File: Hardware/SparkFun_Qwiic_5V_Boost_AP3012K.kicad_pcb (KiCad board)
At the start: 2 copper layers, 25.4 x 25.4 mm, 65 parts, among them J1 Qwiic_RA, J2 Qwiic_RA, J3 Conn_01x06, Q1 BSS138, Q2 BSS138, U5 AP3012

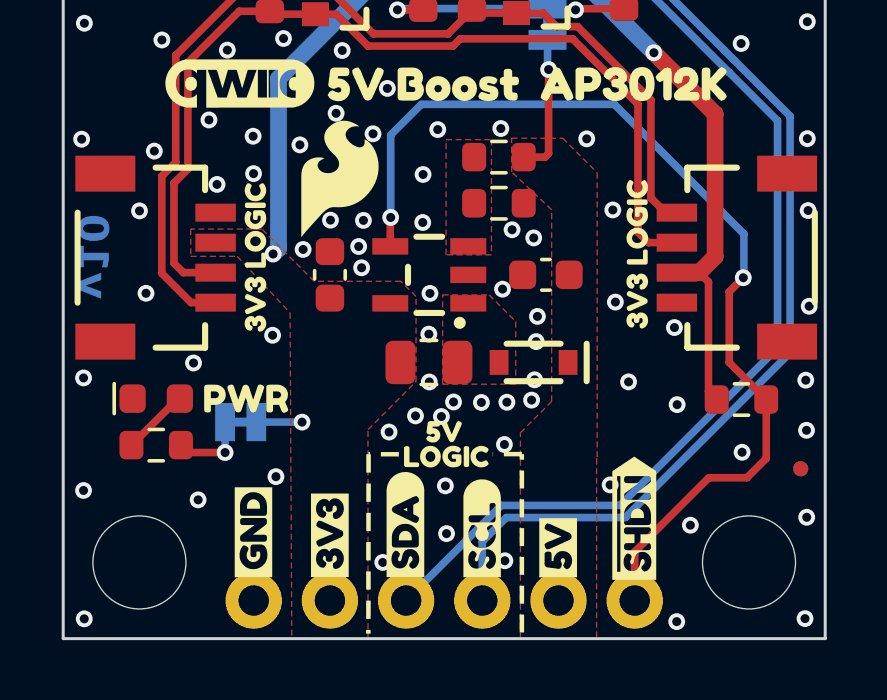
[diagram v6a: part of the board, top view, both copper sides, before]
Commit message: buzzard label adjustments
-extended left side spacing of PTH buzzard labels to 6mils
-positioned them so they clear the PTH header plastic molding courtyard
-snapped them all to a 6.25mils grid.
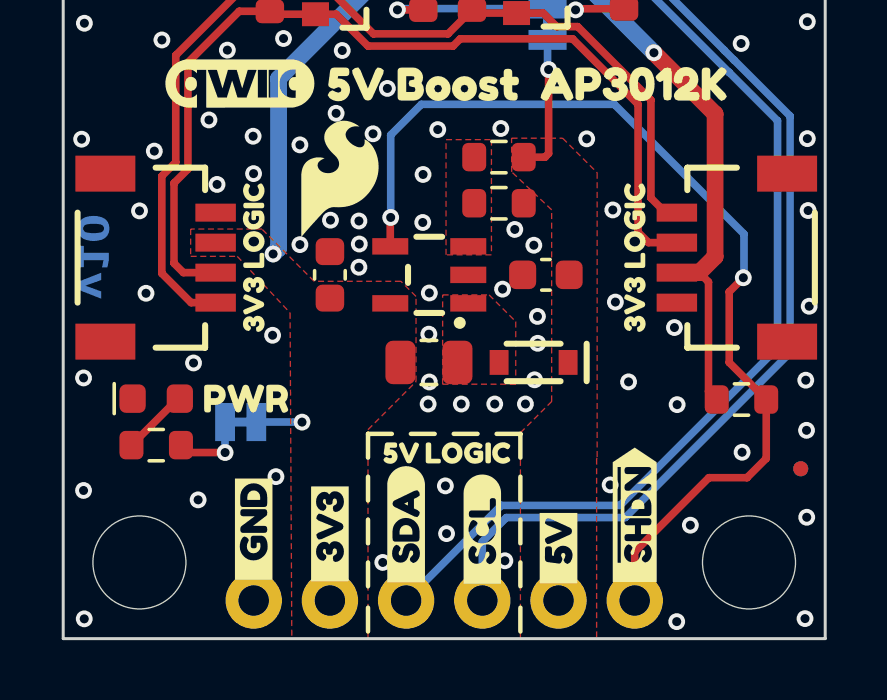
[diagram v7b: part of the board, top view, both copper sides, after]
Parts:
- removed kibuzzard-67A5185F: G***, kibuzzard-67A5185F
- removed kibuzzard-67A5186C: G***, kibuzzard-67A5186C
- removed kibuzzard-67A51876: G***, kibuzzard-67A51876
- removed kibuzzard-67A51896: G***, kibuzzard-67A51896
- removed kibuzzard-67A518A8: G***, kibuzzard-67A518A8
- removed kibuzzard-67A518C6: G***, kibuzzard-67A518C6
- removed kibuzzard-67A519AE: G***, kibuzzard-67A519AE
- removed kibuzzard-67A519C3: G***, kibuzzard-67A519C3
- removed kibuzzard-67A519FE: G***, kibuzzard-67A519FE
- removed kibuzzard-67A51A0B: G***, kibuzzard-67A51A0B
- removed kibuzzard-67A51A19: G***, kibuzzard-67A51A19
- removed kibuzzard-67A51A2F: G***, kibuzzard-67A51A2F
- added kibuzzard-67BF7C99: G***, kibuzzard-67BF7C99, F.Cu at (129.6, 107.2)
- added kibuzzard-67BF7CAB: G***, kibuzzard-67BF7CAB, F.Cu at (132.2, 107.3)
- added kibuzzard-67BF7CFE: G***, kibuzzard-67BF7CFE, F.Cu at (134.7, 107.0)
- added kibuzzard-67BF7D12: G***, kibuzzard-67BF7D12, F.Cu at (137.2, 107.2)
- added kibuzzard-67BF7D5E: G***, kibuzzard-67BF7D5E, F.Cu at (139.8, 107.8)
- added kibuzzard-67BF7D85: G***, kibuzzard-67BF7D85, F.Cu at (142.3, 106.7)
- added kibuzzard-67BF7EBF: G***, kibuzzard-67BF7EBF, B.Cu at (129.6, 107.2)
- added kibuzzard-67BF7ED9: G***, kibuzzard-67BF7ED9, B.Cu at (132.2, 107.3)
- added kibuzzard-67BF7F13: G***, kibuzzard-67BF7F13, B.Cu at (134.7, 107.0)
- added kibuzzard-67BF7F2F: G***, kibuzzard-67BF7F2F, B.Cu at (137.2, 107.2)
- added kibuzzard-67BF7F4D: G***, kibuzzard-67BF7F4D, B.Cu at (139.8, 107.8)
- added kibuzzard-67BF7F7D: G***, kibuzzard-67BF7F7D, B.Cu at (142.3, 106.7)
- moved kibuzzard-67BF5EEE 1.68 mm to (137.6, 104.6)
- moved kibuzzard-67BF5EEE 1.59 mm to (134.5, 104.6)
- moved kibuzzard-67BF5EF7 0.73 mm to (136.8, 104.6)
- moved kibuzzard-67BF5EF7 0.64 mm to (135.3, 104.6)
- moved kibuzzard-67BF5F1D 0.14 mm to (142.3, 98.1)
- moved kibuzzard-67BF5F1D 0.06 mm to (129.6, 98.1)
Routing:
- net GND: vias 83 -> 79

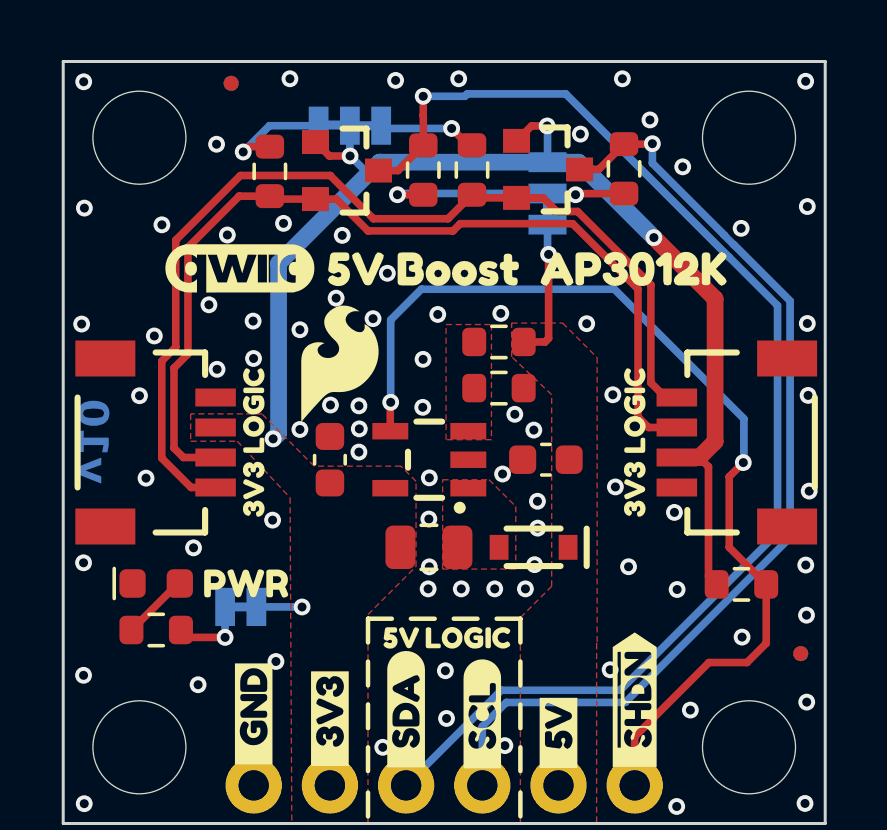
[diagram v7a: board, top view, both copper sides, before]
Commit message: moving parts onto 12.5mil grid
-moved parts (except the boost circuit stuff) onto the 12.5 mil grid.
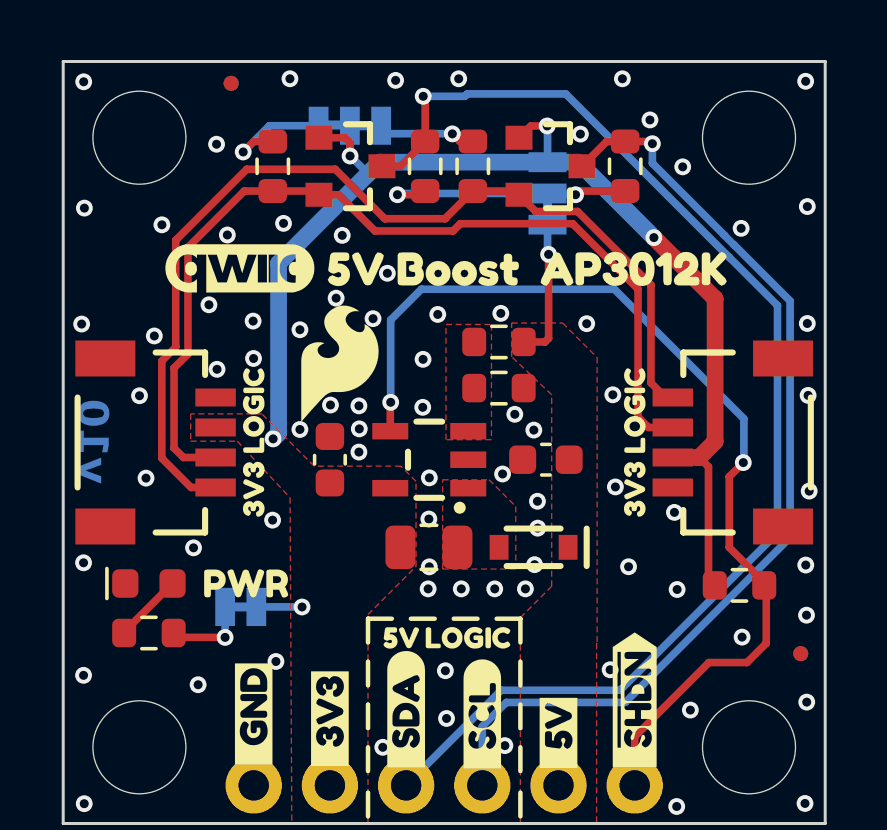
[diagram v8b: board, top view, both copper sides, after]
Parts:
- moved R3 0.26 mm to (126.1, 104.5)
- moved D1 0.24 mm to (126.1, 102.8)
- moved R4 0.20 mm to (130.3, 88.9)
- moved Q2 0.18 mm to (132.8, 88.9)
- moved R7 0.14 mm to (135.3, 88.9)
- moved J1 0.13 mm to (143.6, 98.1)
- moved Q1 0.13 mm to (139.5, 88.9)
- moved R5 0.13 mm to (136.9, 88.9)
- moved R8 0.09 mm to (142.0, 88.9)
- moved R6 0.07 mm to (145.8, 102.9)
